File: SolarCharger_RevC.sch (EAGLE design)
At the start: 123 parts, among them CON1 CON_4X200MIL, CON2 USB_BMULTICOMP, CON3 ICSP, CON4 CON_3X100MIL, CON5 CON_3X100MIL, CON6 CON_8X200MIL, CON7 CON_2X100MIL, IC1 MCP3428, IC10 S25FL208K, IC11 TPS54428, IC12 MCP14A0153, IC13 MCP14A0153, IC2 INA213LONG, IC3 MIC4605-1YM, IC4 INA213LONG, IC5 PIC18F46J50, IC6 TS6001, IC7 LMT86, IC8 24AA16, IC9 TPS62120, Q1 NX3008NBKW, Q10 NTR4101PT1G, Q11 N-FET, Q12 N-FET, Q13 N-FET, Q14 N-FET, Q15 NX3008NBKW, Q2 PSMN6R0-30YL, Q3 NX3008NBKW, Q4 NTR4101PT1G, Q5 PSMN6R0-30YL, Q6 PSMN6R0-30YL, Q7 NX3008NBKW, Q8 NX3008NBKW, Q9 NX3008NBKW, X1 ABS07-120-32.768KHZ-T, X2 ABM3-8.000MHZ-D2Y-T, X3 USB_A, X4 USB_A

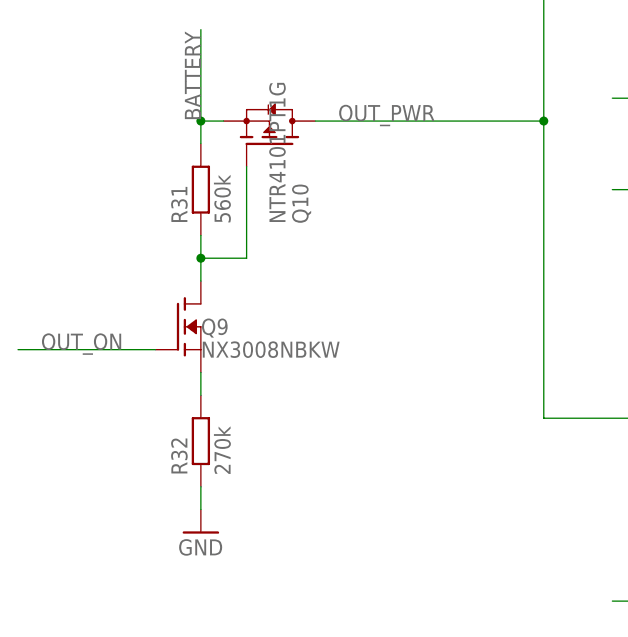
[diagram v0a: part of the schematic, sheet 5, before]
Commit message: Some resistor values fixed
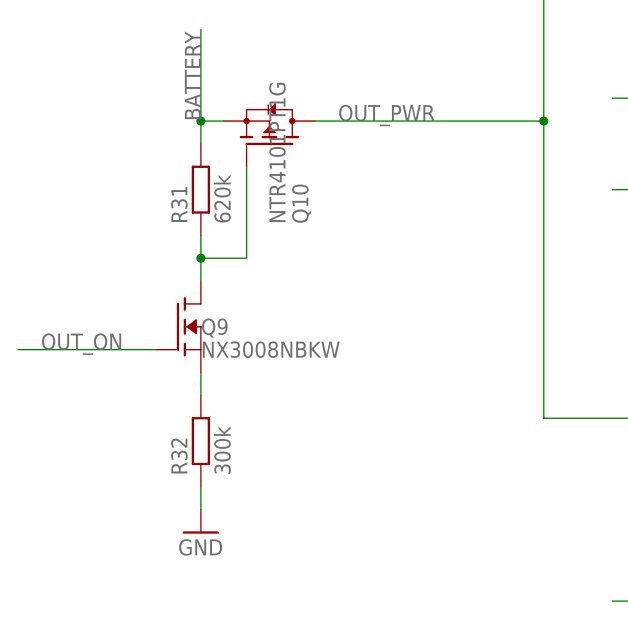
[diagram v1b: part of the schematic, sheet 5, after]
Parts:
- R31: value 560k -> 620k
- R32: value 270k -> 300k
- R6: value 22 -> 5R6
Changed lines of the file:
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@@
 <part name="Q10" library="00Mosfet" deviceset="P-FET" device="SOT23" value="NTR4101PT1G"/>
 <part name="GND69" library="supply1" deviceset="GND" device=""/>
-<part name="R31" library="00Resistor" deviceset="RESISTOR" device="R0805" value="560k"/>
-<part name="R32" library="00Resistor" deviceset="RESISTOR" device="R0805" value="270k"/>
+<part name="R31" library="00Resistor" deviceset="RESISTOR" device="R0805" value="620k"/>
+<part name="R32" library="00Resistor" deviceset="RESISTOR" device="R0805" value="300k"/>
 <part name="Q1" library="00Mosfet" deviceset="N-FET" device="SOT23" value="NX3008NBKW"/>
 <part name="C5" library="00Capacitor" deviceset="C_POLARIZED" device="10MM" value="470u 25V"/>
@@
 <part name="GND14" library="supply1" deviceset="GND" device=""/>
 <part name="Q3" library="00Mosfet" deviceset="N-FET" device="SOT23" value="NX3008NBKW"/>
-<part name="R6" library="00Resistor" deviceset="RESISTOR" device="R0805" value="22"/>
+<part name="R6" library="00Resistor" deviceset="RESISTOR" device="R0805" value="5R6"/>
 <part name="CON3" library="00Connector" deviceset="CON_6X" device="100MIL" value="ICSP"/>
 <part name="IC5" library="00PIC" deviceset="PIC18F46J50" device=""/>

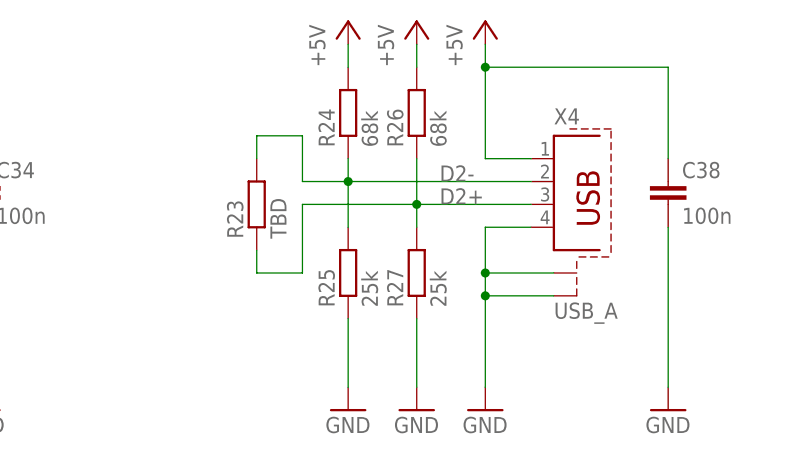
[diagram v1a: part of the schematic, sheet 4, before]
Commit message: Some resistor values changed
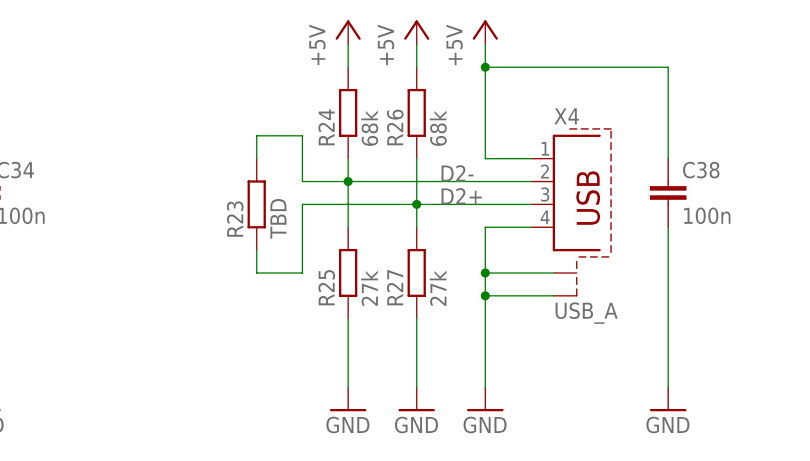
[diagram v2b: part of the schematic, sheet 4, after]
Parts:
- R25, R27: value 25k -> 27k
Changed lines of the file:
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@@
 <part name="P+14" library="00Supply" deviceset="+5V" device=""/>
 <part name="R23" library="00Resistor" deviceset="RESISTOR" device="R0805" value="TBD"/>
-<part name="R25" library="00Resistor" deviceset="RESISTOR" device="R0805" value="25k"/>
-<part name="R27" library="00Resistor" deviceset="RESISTOR" device="R0805" value="25k"/>
+<part name="R25" library="00Resistor" deviceset="RESISTOR" device="R0805" value="27k"/>
+<part name="R27" library="00Resistor" deviceset="RESISTOR" device="R0805" value="27k"/>
 <part name="R26" library="00Resistor" deviceset="RESISTOR" device="R0805" value="68k"/>
 <part name="R24" library="00Resistor" deviceset="RESISTOR" device="R0805" value="68k"/>
